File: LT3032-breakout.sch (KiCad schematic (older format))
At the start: 9 parts, among them J1 CONN_01X03, J2 CONN_01X03, U1 LT3032-X

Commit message: Removed unused libraries Added component names
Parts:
- C1, C2, C5, C6: MFN (none) -> Taiyo Yuden; MFP (none) -> GMK325BJ106KN-T
- C3, C4: MFN (none) -> Kemet; MFP (none) -> C0603C100J5GACTU
- J1, J2: MFN (none) -> TE Connectivity; MFP (none) -> 4-103741-0
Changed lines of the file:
@@
 LIBS:contrib
 LIBS:valves
-LIBS:ADI
-LIBS:Texas Instruments
 LIBS:Linear Technology
 LIBS:LT3032-breakout-cache
@@
 F 2 "Capacitors_SMD:C_1210" H 4450 3300 50  0001 C CNN
 F 3 "" H 4450 3300 50  0000 C CNN
+F 4 "Taiyo Yuden" H 4450 3300 60  0001 C CNN "MFN"
+F 5 "GMK325BJ106KN-T" H 4450 3300 60  0001 C CNN "MFP"
 	1    4450 3300
 	1    0    0    1
@@
 F 2 "Capacitors_SMD:C_1210" H 4450 3700 50  0001 C CNN
 F 3 "" H 4450 3700 50  0000 C CNN
+F 4 "Taiyo Yuden" H 4450 3700 60  0001 C CNN "MFN"
+F 5 "GMK325BJ106KN-T" H 4450 3700 60  0001 C CNN "MFP"
 	1    4450 3700
 	1    0    0    1
@@
 F 2 "Capacitors_SMD:C_0603" H 6900 3050 50  0001 C CNN
 F 3 "" H 6900 3050 50  0000 C CNN
+F 4 "Kemet" H 6900 3050 60  0001 C CNN "MFN"
+F 5 "C0603C100J5GACTU" H 6900 3050 60  0001 C CNN "MFP"
 	1    6900 3050
 	1    0    0    1
@@
 F 2 "Capacitors_SMD:C_0603" H 6900 3950 50  0001 C CNN
 F 3 "" H 6900 3950 50  0000 C CNN
+F 4 "Kemet" H 6900 3950 60  0001 C CNN "MFN"
+F 5 "C0603C100J5GACTU" H 6900 3950 60  0001 C CNN "MFP"
 	1    6900 3950
 	1    0    0    1
@@
 F 2 "Capacitors_SMD:C_1210" H 7400 3050 50  0001 C CNN
 F 3 "" H 7400 3050 50  0000 C CNN
+F 4 "Taiyo Yuden" H 7400 3050 60  0001 C CNN "MFN"
+F 5 "GMK325BJ106KN-T" H 7400 3050 60  0001 C CNN "MFP"
 	1    7400 3050
 	1    0    0    1
@@
 F 2 "Capacitors_SMD:C_1210" H 7400 3950 50  0001 C CNN
 F 3 "" H 7400 3950 50  0000 C CNN
+F 4 "Taiyo Yuden" H 7400 3950 60  0001 C CNN "MFN"
+F 5 "GMK325BJ106KN-T" H 7400 3950 60  0001 C CNN "MFP"
 	1    7400 3950
 	1    0    0    1
@@
 Connection ~ 4450 3500
 $Comp
-L GND #PWR2
+L GND #PWR01
 U 1 1 5962442E
 P 5800 4250
-F 0 "#PWR2" H 5800 4000 50  0001 C CNN
+F 0 "#PWR01" H 5800 4000 50  0001 C CNN
 F 1 "GND" H 5800 4100 50  0000 C CNN
 F 2 "" H 5800 4250 50  0000 C CNN
@@
 Connection ~ 7400 3450
 $Comp
-L GND #PWR3
+L GND #PWR02
 U 1 1 59628009
 P 7250 3500
-F 0 "#PWR3" H 7250 3250 50  0001 C CNN
+F 0 "#PWR02" H 7250 3250 50  0001 C CNN
 F 1 "GND" H 7250 3350 50  0000 C CNN
 F 2 "" H 7250 3500 50  0000 C CNN
@@
 Connection ~ 7400 2800
 $Comp
-L GND #PWR1
+L GND #PWR03
 U 1 1 595F4C00
 P 4700 3550
-F 0 "#PWR1" H 4700 3300 50  0001 C CNN
+F 0 "#PWR03" H 4700 3300 50  0001 C CNN
 F 1 "GND" H 4700 3400 50  0000 C CNN
 F 2 "" H 4700 3550 50  0000 C CNN
@@
 F 2 "Pin_Headers:Pin_Header_Straight_1x03_Pitch2.54mm" H 3550 3500 50  0001 C CNN
 F 3 "" H 3550 3500 50  0001 C CNN
+F 4 "TE Connectivity" H 3550 3500 60  0001 C CNN "MFN"
+F 5 "4-103741-0" H 3550 3500 60  0001 C CNN "MFP"
 	1    3550 3500
 	-1   0    0    -1
@@
 F 2 "Pin_Headers:Pin_Header_Straight_1x03_Pitch2.54mm" H 8300 3450 50  0001 C CNN
 F 3 "" H 8300 3450 50  0001 C CNN
+F 4 "TE Connectivity" H 8300 3450 60  0001 C CNN "MFN"
+F 5 "4-103741-0" H 8300 3450 60  0001 C CNN "MFP"
 	1    8300 3450
 	1    0    0    -1

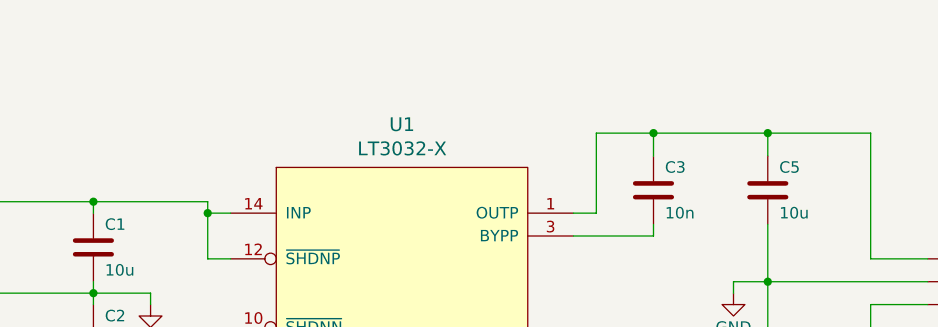
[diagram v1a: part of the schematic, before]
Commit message: Added a note to make it more clear that only fixed voltage regulators are supported
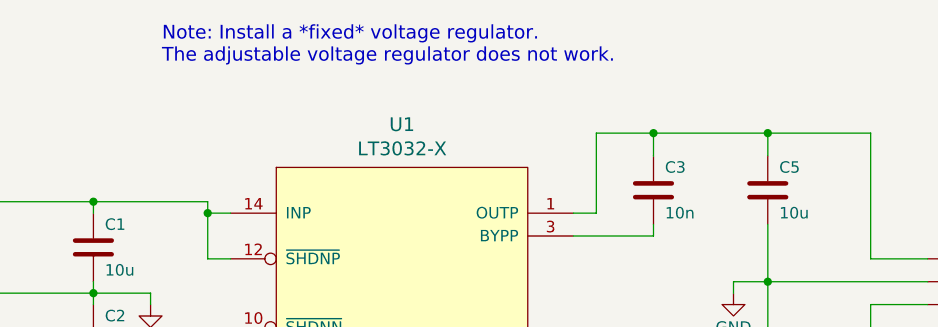
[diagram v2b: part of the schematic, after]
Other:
- note added: "Note: Install a *fixed* voltage regulator.\nThe adjustable voltage regulator does not work."
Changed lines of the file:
@@
 Wire Wire Line
 	7850 3550 7850 4200
+Text Notes 4750 2500 0    60   ~ 0
+Note: Install a *fixed* voltage regulator.\nThe adjustable voltage regulator does not work.
 $EndSCHEMATC

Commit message: Updated libraries
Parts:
- C3, C4: MFN Kemet -> Murata; MFP C0603C100J5GACTU -> GRM1885C1E103GA01D; Note (none) -> Use C0G
- U1: footprint Custom_footprints:DFN-14-1EP_3x4mm_Pitch0.5mm_2Pads -> Custom_footprints:DFN-14-2EP_3x4mm_Pitch0.5mm
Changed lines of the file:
@@
 F 2 "Capacitors_SMD:C_0603" H 6900 3050 50  0001 C CNN
 F 3 "" H 6900 3050 50  0000 C CNN
-F 4 "Kemet" H 6900 3050 60  0001 C CNN "MFN"
-F 5 "C0603C100J5GACTU" H 6900 3050 60  0001 C CNN "MFP"
+F 4 "Murata" H 6900 3050 60  0001 C CNN "MFN"
+F 5 "GRM1885C1E103GA01D" H 6900 3050 60  0001 C CNN "MFP"
+F 6 "Use C0G" H 6900 3050 60  0001 C CNN "Note"
 	1    6900 3050
 	1    0    0    1
@@
 F 2 "Capacitors_SMD:C_0603" H 6900 3950 50  0001 C CNN
 F 3 "" H 6900 3950 50  0000 C CNN
-F 4 "Kemet" H 6900 3950 60  0001 C CNN "MFN"
-F 5 "C0603C100J5GACTU" H 6900 3950 60  0001 C CNN "MFP"
+F 4 "Murata" H 6900 3950 60  0001 C CNN "MFN"
+F 5 "GRM1885C1E103GA01D" H 6900 3950 60  0001 C CNN "MFP"
+F 6 "Use C0G" H 6900 3950 60  0001 C CNN "Note"
 	1    6900 3950
 	1    0    0    1
@@
 F 0 "U1" H 5800 4237 60  0000 C CNN
 F 1 "LT3032-X" H 5800 4131 60  0000 C CNN
-F 2 "Custom_footprints:DFN-14-1EP_3x4mm_Pitch0.5mm_2Pads" H 5800 4300 60  0001 C CNN
+F 2 "Custom_footprints:DFN-14-2EP_3x4mm_Pitch0.5mm" H 5800 4300 60  0001 C CNN
 F 3 "" H 5800 4150 60  0001 C CNN
 F 4 "Linear Technology" H 6550 2900 60  0001 C CNN "MFN"

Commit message: Updated libraries Added schematic as PDF
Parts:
- J1: value CONN_01X03 -> Input; symbol CONN_01X03 -> Conn_01x03
- J2: value CONN_01X03 -> Output; symbol CONN_01X03 -> Conn_01x03
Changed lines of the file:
@@
 Connection ~ 4950 3850
 $Comp
-L CONN_01X03 J1
+L Conn_01x03 J1
 U 1 1 59836410
 P 3550 3500
 F 0 "J1" H 3628 3541 50  0000 L CNN
-F 1 "CONN_01X03" H 3628 3450 50  0000 L CNN
+F 1 "Input" H 3628 3450 50  0000 L CNN
 F 2 "Pin_Headers:Pin_Header_Straight_1x03_Pitch2.54mm" H 3550 3500 50  0001 C CNN
 F 3 "" H 3550 3500 50  0001 C CNN
@@
 	4000 3900 4950 3900
 $Comp
-L CONN_01X03 J2
+L Conn_01x03 J2
 U 1 1 598367F2
 P 8300 3450
 F 0 "J2" H 8378 3491 50  0000 L CNN
-F 1 "CONN_01X03" H 8378 3400 50  0000 L CNN
+F 1 "Output" H 8378 3400 50  0000 L CNN
 F 2 "Pin_Headers:Pin_Header_Straight_1x03_Pitch2.54mm" H 8300 3450 50  0001 C CNN
 F 3 "" H 8300 3450 50  0001 C CNN

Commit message: Updated schematic to KiCAD v5.0
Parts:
- C1, C2, C5, C6: footprint Capacitors_SMD:C_1210 -> Capacitor_SMD:C_1210_3225Metric; symbol C -> Device:C
- C3, C4: footprint Capacitors_SMD:C_0603 -> Capacitor_SMD:C_0603_1608Metric; symbol C -> Device:C; MFP GRM1885C1E103GA01D -> GRM1885C1H103JA01J
- J1, J2: footprint Pin_Headers:Pin_Header_Straight_1x03_Pitch2.54mm -> Connector_PinHeader_2.54mm:PinHeader_1x03_P2.54mm_Vertical; symbol Conn_01x03 -> Connector_Generic:Conn_01x03
- U1: footprint Custom_footprints:DFN-14-2EP_3x4mm_Pitch0.5mm -> Package_DFN_QFN:Linear_DE14MA; symbol LT3032-X -> Linear-Technology:LT3032-X
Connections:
- net labels added: INN, INP
- wire segments 39 -> 51
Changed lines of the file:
@@
-EESchema Schematic File Version 2
-LIBS:power
-LIBS:device
-LIBS:transistors
-LIBS:conn
-LIBS:linear
-LIBS:regul
-LIBS:74xx
-LIBS:cmos4000
-LIBS:adc-dac
-LIBS:memory
-LIBS:xilinx
-LIBS:microcontrollers
-LIBS:dsp
-LIBS:microchip
-LIBS:analog_switches
-LIBS:motorola
-LIBS:texas
-LIBS:intel
-LIBS:audio
-LIBS:interface
-LIBS:digital-audio
-LIBS:philips
-LIBS:display
-LIBS:cypress
-LIBS:siliconi
-LIBS:opto
-LIBS:atmel
-LIBS:contrib
-LIBS:valves
-LIBS:Linear Technology
+EESchema Schematic File Version 4
 LIBS:LT3032-breakout-cache
 EELAYER 26 0
@@
 $EndDescr
 $Comp
-L C C1
+L Device:C C1
 U 1 1 59577699
 P 4450 3300
 F 0 "C1" H 4500 3200 50  0000 L CNN
 F 1 "10u" H 4500 3400 50  0000 L CNN
-F 2 "Capacitors_SMD:C_1210" H 4450 3300 50  0001 C CNN
+F 2 "Capacitor_SMD:C_1210_3225Metric" H 4450 3300 50  0001 C CNN
 F 3 "" H 4450 3300 50  0000 C CNN
 F 4 "Taiyo Yuden" H 4450 3300 60  0001 C CNN "MFN"
@@
 $EndComp
 $Comp
-L C C2
+L Device:C C2
 U 1 1 595783CE
 P 4450 3700
 F 0 "C2" H 4500 3600 50  0000 L CNN
 F 1 "10u" H 4500 3800 50  0000 L CNN
-F 2 "Capacitors_SMD:C_1210" H 4450 3700 50  0001 C CNN
+F 2 "Capacitor_SMD:C_1210_3225Metric" H 4450 3700 50  0001 C CNN
 F 3 "" H 4450 3700 50  0000 C CNN
 F 4 "Taiyo Yuden" H 4450 3700 60  0001 C CNN "MFN"
@@
 $EndComp
 $Comp
-L C C3
+L Device:C C3
 U 1 1 59579123
 P 6900 3050
 F 0 "C3" H 6950 2950 50  0000 L CNN
 F 1 "10n" H 6950 3150 50  0000 L CNN
-F 2 "Capacitors_SMD:C_0603" H 6900 3050 50  0001 C CNN
+F 2 "Capacitor_SMD:C_0603_1608Metric" H 6900 3050 50  0001 C CNN
 F 3 "" H 6900 3050 50  0000 C CNN
 F 4 "Murata" H 6900 3050 60  0001 C CNN "MFN"
-F 5 "GRM1885C1E103GA01D" H 6900 3050 60  0001 C CNN "MFP"
+F 5 "GRM1885C1H103JA01J" H 6900 3050 60  0001 C CNN "MFP"
 F 6 "Use C0G" H 6900 3050 60  0001 C CNN "Note"
 	1    6900 3050
@@
 $EndComp
 $Comp
-L C C4
+L Device:C C4
 U 1 1 595791FF
 P 6900 3950
 F 0 "C4" H 6950 3850 50  0000 L CNN
 F 1 "10n" H 6950 4050 50  0000 L CNN
-F 2 "Capacitors_SMD:C_0603" H 6900 3950 50  0001 C CNN
+F 2 "Capacitor_SMD:C_0603_1608Metric" H 6900 3950 50  0001 C CNN
 F 3 "" H 6900 3950 50  0000 C CNN
 F 4 "Murata" H 6900 3950 60  0001 C CNN "MFN"
-F 5 "GRM1885C1E103GA01D" H 6900 3950 60  0001 C CNN "MFP"
+F 5 "GRM1885C1H103JA01J" H 6900 3950 60  0001 C CNN "MFP"
 F 6 "Use C0G" H 6900 3950 60  0001 C CNN "Note"
 	1    6900 3950
@@
 $EndComp
 $Comp
-L C C5
+L Device:C C5
 U 1 1 595798C2
 P 7400 3050
 F 0 "C5" H 7450 2950 50  0000 L CNN
 F 1 "10u" H 7450 3150 50  0000 L CNN
-F 2 "Capacitors_SMD:C_1210" H 7400 3050 50  0001 C CNN
+F 2 "Capacitor_SMD:C_1210_3225Metric" H 7400 3050 50  0001 C CNN
 F 3 "" H 7400 3050 50  0000 C CNN
 F 4 "Taiyo Yuden" H 7400 3050 60  0001 C CNN "MFN"
@@
 $EndComp
 $Comp
-L C C6
+L Device:C C6
 U 1 1 595799A0
 P 7400 3950
 F 0 "C6" H 7450 3850 50  0000 L CNN
 F 1 "10u" H 7450 4050 50  0000 L CNN
-F 2 "Capacitors_SMD:C_1210" H 7400 3950 50  0001 C CNN
+F 2 "Capacitor_SMD:C_1210_3225Metric" H 7400 3950 50  0001 C CNN
 F 3 "" H 7400 3950 50  0000 C CNN
 F 4 "Taiyo Yuden" H 7400 3950 60  0001 C CNN "MFN"
@@
 $EndComp
 $Comp
-L LT3032-X U1
+L Linear-Technology:LT3032-X U1
 U 1 1 59620D90
 P 5800 3500
 F 0 "U1" H 5800 4237 60  0000 C CNN
 F 1 "LT3032-X" H 5800 4131 60  0000 C CNN
-F 2 "Custom_footprints:DFN-14-2EP_3x4mm_Pitch0.5mm" H 5800 4300 60  0001 C CNN
+F 2 "Package_DFN_QFN:Linear_DE14MA" H 5800 4300 60  0001 C CNN
 F 3 "" H 5800 4150 60  0001 C CNN
 F 4 "Linear Technology" H 6550 2900 60  0001 C CNN "MFN"
@@
 	5050 3150 4950 3150
 Wire Wire Line
-	4000 3100 4950 3100
+	4000 3100 4450 3100
 Wire Wire Line
 	4450 3150 4450 3100
@@
 	5050 3850 4950 3850
 Wire Wire Line
-	4950 3900 4950 3650
+	4950 3900 4950 3850
 Wire Wire Line
 	4450 3850 4450 3900
 Connection ~ 4450 3900
 Wire Wire Line
-	4450 3450 4450 3550
-Wire Wire Line
-	3750 3500 4700 3500
+	4450 3450 4450 3500
+Wire Wire Line
+	3750 3500 4450 3500
 Connection ~ 4450 3500
 $Comp
-L GND #PWR01
+L power:GND #PWR01
 U 1 1 5962442E
 P 5800 4250
@@
 	6650 3150 6650 2800
 Wire Wire Line
-	6650 2800 7850 2800
+	6650 2800 6900 2800
 Wire Wire Line
 	7400 2800 7400 2900
@@
 	6650 3850 6650 4200
 Wire Wire Line
-	6650 4200 7850 4200
+	6650 4200 6900 4200
 Wire Wire Line
 	6900 4200 6900 4100
@@
 Connection ~ 6900 4200
 Wire Wire Line
-	7400 3200 7400 3800
-Wire Wire Line
-	7250 3450 8100 3450
+	7400 3200 7400 3450
+Wire Wire Line
+	7250 3450 7400 3450
 Wire Wire Line
 	7250 3450 7250 3500
 Connection ~ 7400 3450
 $Comp
-L GND #PWR02
+L power:GND #PWR02
 U 1 1 59628009
 P 7250 3500
@@
 Connection ~ 7400 2800
 $Comp
-L GND #PWR03
+L power:GND #PWR03
 U 1 1 595F4C00
 P 4700 3550
@@
 	4700 3500 4700 3550
 Wire Wire Line
-	4950 3100 4950 3350
+	4950 3100 4950 3150
 Wire Wire Line
 	4950 3350 5050 3350
 Connection ~ 4950 3850
 $Comp
-L Conn_01x03 J1
+L Connector_Generic:Conn_01x03 J1
 U 1 1 59836410
 P 3550 3500
 F 0 "J1" H 3628 3541 50  0000 L CNN
 F 1 "Input" H 3628 3450 50  0000 L CNN
-F 2 "Pin_Headers:Pin_Header_Straight_1x03_Pitch2.54mm" H 3550 3500 50  0001 C CNN
+F 2 "Connector_PinHeader_2.54mm:PinHeader_1x03_P2.54mm_Vertical" H 3550 3500 50  0001 C CNN
 F 3 "" H 3550 3500 50  0001 C CNN
 F 4 "TE Connectivity" H 3550 3500 60  0001 C CNN "MFN"
@@
 	4000 3600 4000 3900
 Wire Wire Line
-	4000 3900 4950 3900
-$Comp
-L Conn_01x03 J2
+	4000 3900 4450 3900
+$Comp
+L Connector_Generic:Conn_01x03 J2
 U 1 1 598367F2
 P 8300 3450
 F 0 "J2" H 8378 3491 50  0000 L CNN
 F 1 "Output" H 8378 3400 50  0000 L CNN
-F 2 "Pin_Headers:Pin_Header_Straight_1x03_Pitch2.54mm" H 8300 3450 50  0001 C CNN
+F 2 "Connector_PinHeader_2.54mm:PinHeader_1x03_P2.54mm_Vertical" H 8300 3450 50  0001 C CNN
 F 3 "" H 8300 3450 50  0001 C CNN
 F 4 "TE Connectivity" H 8300 3450 60  0001 C CNN "MFN"
@@
 Text Notes 4750 2500 0    60   ~ 0
 Note: Install a *fixed* voltage regulator.\nThe adjustable voltage regulator does not work.
+Wire Wire Line
+	4450 3100 4950 3100
+Wire Wire Line
+	4450 3900 4950 3900
+Wire Wire Line
+	4450 3500 4450 3550
+Wire Wire Line
+	4450 3500 4700 3500
+Wire Wire Line
+	4950 3150 4950 3350
+Wire Wire Line
+	6900 2800 7400 2800
+Wire Wire Line
+	6900 4200 7400 4200
+Wire Wire Line
+	7400 3450 7400 3800
+Wire Wire Line
+	7400 3450 8100 3450
+Wire Wire Line
+	7400 4200 7850 4200
+Wire Wire Line
+	7400 2800 7850 2800
+Wire Wire Line
+	4950 3850 4950 3650
+Text Label 4100 3900 0    60   ~ 0
+INN
+Text Label 4100 3100 0    60   ~ 0
+INP
+$Comp
+L Graphic:Logo_Open_Hardware_Small #LOGO1
+U 1 1 5B03B1EC
+P 10550 6200
+F 0 "#LOGO1" H 10550 6475 50  0001 C CNN
+F 1 "Logo_Open_Hardware_Small" H 10550 5975 50  0001 C CNN
+F 2 "Symbol:OSHW-Logo_7.5x8mm_SilkScreen" H 10550 6200 50  0001 C CNN
+F 3 "~" H 10550 6200 50  0001 C CNN
+	1    10550 6200
+	1    0    0    -1
+$EndComp
 $EndSCHEMATC
